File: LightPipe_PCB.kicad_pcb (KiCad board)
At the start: 4 copper layers, 38 x 38 mm, 14 parts, among them M1 2.2mm_M2, M2 2.2mm_M2, X1 AudioJack4, X2 AudioJack4, X3 XT30, X4.1 Cable-0.7mm, X4.2 Cable-0.7mm, X5.1 Cable-1.5mm, X5.2 Cable-1.5mm

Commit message: [PCB] Fixed Fab layers | added attributes to components
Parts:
- X1, X2: value AudioJack4 -> Lumberg KLB4
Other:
- rule pad_to_mask_clearance: 0.051 -> 0
- board text removed: "Rotationswinkel: 120° 60° 10°"
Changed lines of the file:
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@@
       (dielectric_constraints no)
     )
-    (pad_to_mask_clearance 0.051)
-    (solder_mask_min_width 0.25)
+    (pad_to_mask_clearance 0)
     (grid_origin 127 90)
     (pcbplotparams
@@
   (footprint "h8-Connectors:Lumberg-KLB-4-Jack-3_5-180deg-turnable" (layer "F.Cu")
     (at 138.691343 96.75 60)
+    (property "MF" "Lumberg")
+    (property "MF1" "HUXUAN")
+    (property "MFN" "KLB4")
+    (property "MFN1" "PJ392")
     (property "Sheetfile" "LightPipe_PCB.kicad_sch")
     (property "Sheetname" "")
@@
       (effects (font (size 1 1) (thickness 0.15)))
     )
-    (fp_text value "AudioJack4" (at 0 -5.5 60) (layer "F.Fab")
+    (fp_text value "Lumberg KLB4" (at 0.185417 -6.678848 60) (layer "F.Fab")
       (effects (font (size 1 1) (thickness 0.15)))
     )
@@
   (footprint "h8-Connectors:Lumberg-KLB-4-Jack-3_5-180deg-turnable" (layer "F.Cu")
     (at 115.308657 96.75 -60)
+    (property "MF" "Lumberg")
+    (property "MF1" "HUXUAN")
+    (property "MFN" "KLB4")
+    (property "MFN1" "PJ392")
     (property "Sheetfile" "LightPipe_PCB.kicad_sch")
     (property "Sheetname" "")
@@
       (effects (font (size 1 1) (thickness 0.15)))
     )
-    (fp_text value "AudioJack4" (at 0 -5.5 -60) (layer "F.Fab")
+    (fp_text value "Lumberg KLB4" (at -0.310417 -6.462341 -60) (layer "F.Fab")
       (effects (font (size 1 1) (thickness 0.15)))
     )
@@
   (footprint "h8-Connectors:XT30" (layer "F.Cu")
     (at 127 75.3)
+    (property "LCSC" "C108769")
+    (property "MF" "Changzhou Amass Elec ")
+    (property "MFN" "XT30UPB30-F.G.*")
     (property "Sheetfile" "LightPipe_PCB.kicad_sch")
     (property "Sheetname" "")
@@
       (effects (font (size 1.2 1.2) (thickness 0.2)))
     )
-    (fp_text value "XT30" (at 0 -3.7) (layer "F.Fab")
+    (fp_text value "XT30" (at 0 -3.3) (layer "F.Fab")
       (effects (font (size 0.8 0.8) (thickness 0.15)))
     )
@@
       (effects (font (size 0.8 0.8) (thickness 0.15)) (justify mirror))
     )
-    (fp_text value "Cable-1.5mm" (at 0 -7 -30 unlocked) (layer "B.Fab")
+    (fp_text value "Cable-1.5mm" (at 2.190227 -0.964746 -30 unlocked) (layer "B.Fab")
       (effects (font (size 0.8 0.8) (thickness 0.15)) (justify mirror))
     )
@@
       (effects (font (size 1 1) (thickness 0.15)) (justify mirror))
     )
-    (fp_text value "APA102" (at 4.5 -0.5 300) (layer "B.Fab")
+    (fp_text value "APA102" (at -1.17981 0.069392 300) (layer "B.Fab")
       (effects (font (size 1 1) (thickness 0.15)) (justify mirror))
     )
@@
       (effects (font (size 0.8 0.8) (thickness 0.15)) (justify mirror))
     )
-    (fp_text value "Cable-1.5mm" (at -0.1 -7 -30 unlocked) (layer "B.Fab")
+    (fp_text value "Cable-1.5mm" (at -2.189582 -1.034138 -30 unlocked) (layer "B.Fab")
       (effects (font (size 0.8 0.8) (thickness 0.15)) (justify mirror))
     )
@@
       (effects (font (size 1 1) (thickness 0.15)) (justify mirror))
     )
-    (fp_text value "APA102" (at 4.5 -0.5 180) (layer "B.Fab")
+    (fp_text value "APA102" (at -1.3 0 180) (layer "B.Fab")
       (effects (font (size 1 1) (thickness 0.15)) (justify mirror))
     )
@@
       (effects (font (size 0.8 0.8) (thickness 0.15)) (justify mirror))
     )
-    (fp_text value "Cable-0.7mm" (at 0.1 -6.400001 -30 unlocked) (layer "B.Fab")
+    (fp_text value "Cable-0.7mm" (at 0.235417 -5.775962 -30 unlocked) (layer "B.Fab")
       (effects (font (size 0.8 0.8) (thickness 0.15)) (justify mirror))
     )
@@
       (effects (font (size 0.8 0.8) (thickness 0.15)) (justify mirror))
     )
-    (fp_text value "Cable-0.7mm" (at 0.1 -6.400001 -30 unlocked) (layer "B.Fab")
+    (fp_text value "Cable-0.7mm" (at -0.208493 -5.577405 -30 unlocked) (layer "B.Fab")
       (effects (font (size 0.8 0.8) (thickness 0.15)) (justify mirror))
     )
@@
       (effects (font (size 1 1) (thickness 0.15)) (justify mirror))
     )
-    (fp_text value "APA102" (at 4.7 0 60) (layer "B.Fab")
+    (fp_text value "APA102" (at -1.30481 -0.285898 60) (layer "B.Fab")
       (effects (font (size 1 1) (thickness 0.15)) (justify mirror))
     )
@@
     (effects (font (size 0.8 0.8) (thickness 0.12)) (justify left))
   )
-  (gr_text "Rotationswinkel:\n120°\n60°\n10°" (at 149.4 85) (layer "Cmts.User")
-    (effects (font (size 0.8 0.8) (thickness 0.15)) (justify left))
-  )
   (segment (start 120.557953 105.842047) (end 116.608657 99.001666) (width 0.25) (layer "B.Cu") (net 1))

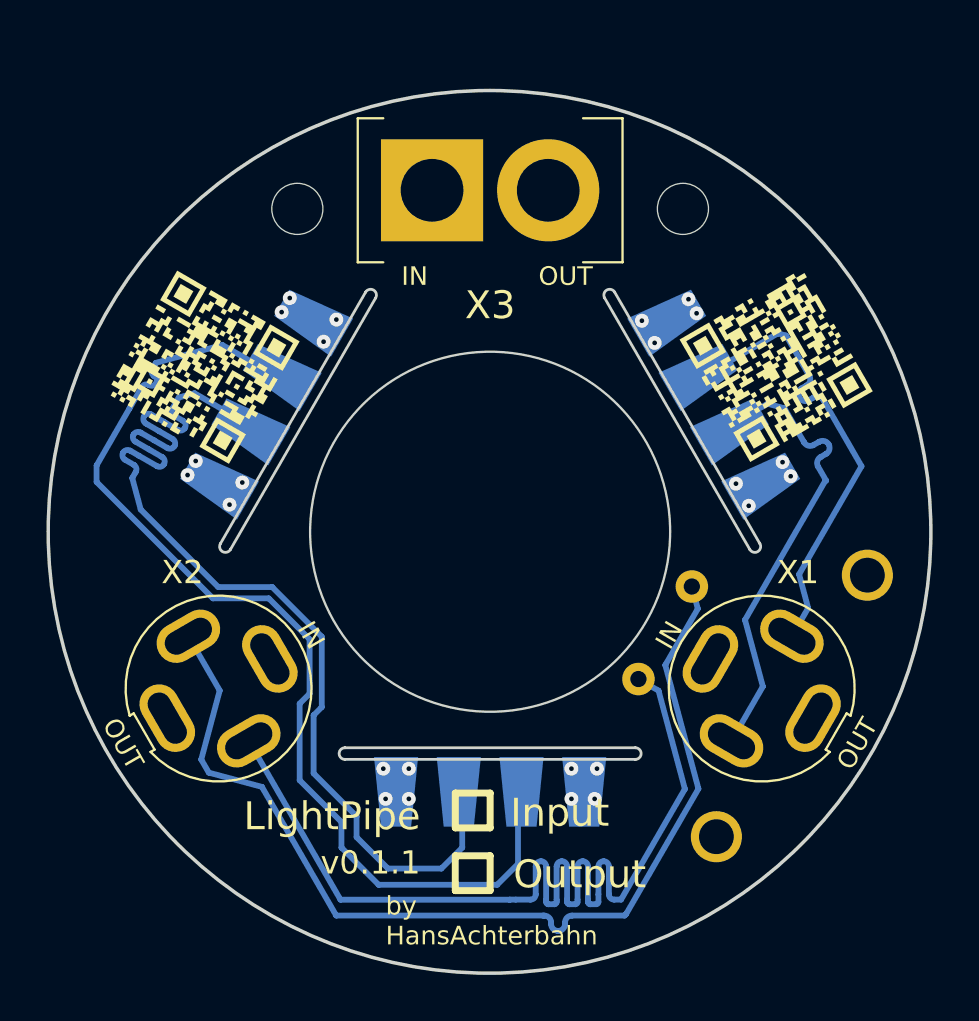
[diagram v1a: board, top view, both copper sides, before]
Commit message: [WIP] Optimize PCB for more common LED-Strip (GND, D, CLK, 5V)
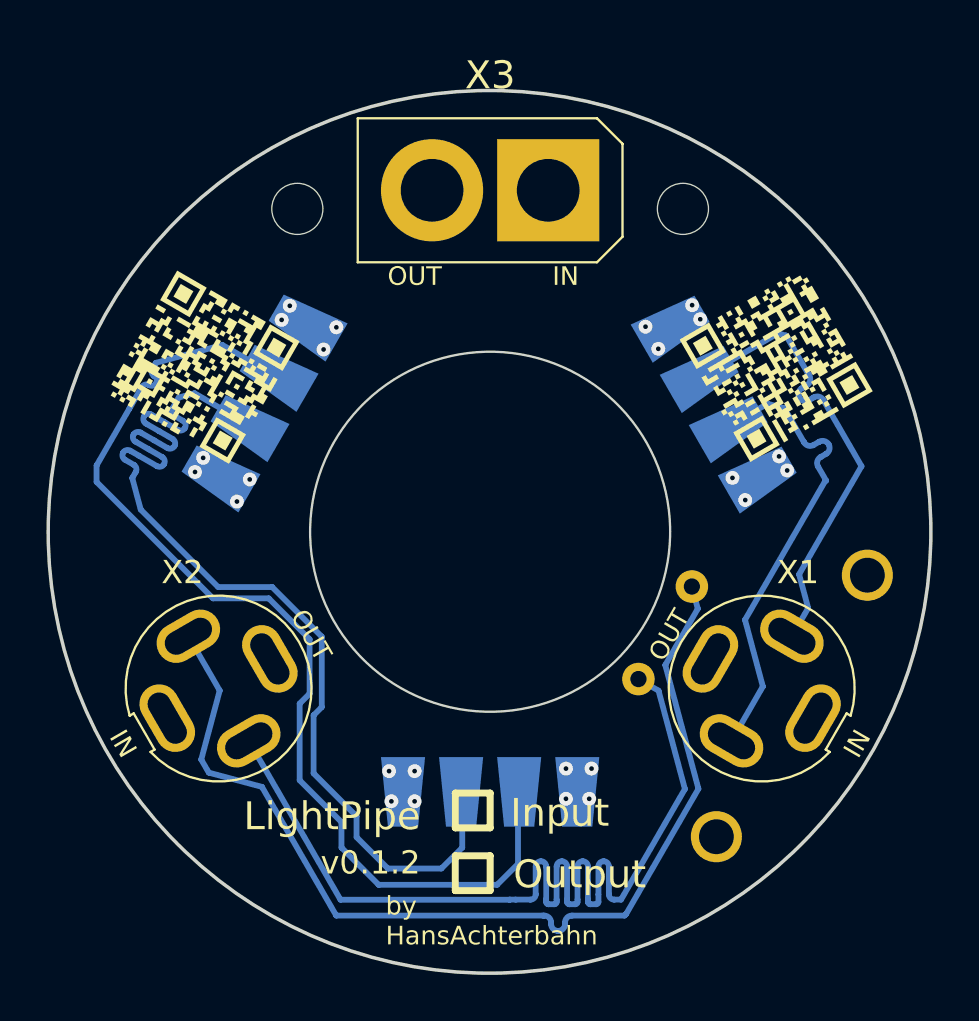
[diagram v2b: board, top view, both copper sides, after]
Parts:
- turned X3 to 180 degrees
- renumbered X5.2 to X5.1, X5.1 to X5.2
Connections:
- LD1 pad 1: +5V -> GND
- LD1 pad 2: /clk1 -> /d1
- LD1 pad 3: /d1 -> /clk1
- LD1 pad 4: GND -> +5V
- LD2 pad 1: +5V -> GND
- LD2 pad 2: /clk2 -> /d2
- LD2 pad 3: /d2 -> /clk2
- LD2 pad 4: GND -> +5V
- LD3 pad 1: +5V -> GND
- LD3 pad 2: /clk2 -> /d2
- LD3 pad 3: /d2 -> /clk2
- LD3 pad 4: GND -> +5V
- X1 pad R1: /clk1 -> /d1
- X1 pad R2: +5V -> GND
- X1 pad S: GND -> +5V
- X1 pad T: /d1 -> /clk1
- X2 pad R1: /clk3 -> /d3
- X2 pad R2: +5V -> GND
- X2 pad S: GND -> +5V
- X2 pad T: /d3 -> /clk3
- X4.1 pad 1: /clk3 -> /d3
- X4.2 pad 1: /d3 -> /clk3
- X5.1 pad 1: GND -> +5V
- X5.2 pad 1: +5V -> GND

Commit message: Optimize PCB for more common LED-Strip (GND, D, CLK, 5V) → It could be a good idea to change X4.1, X4.2, X5.1 and X5.2 to a standard footprint. There is always trouble with this custom footprints.
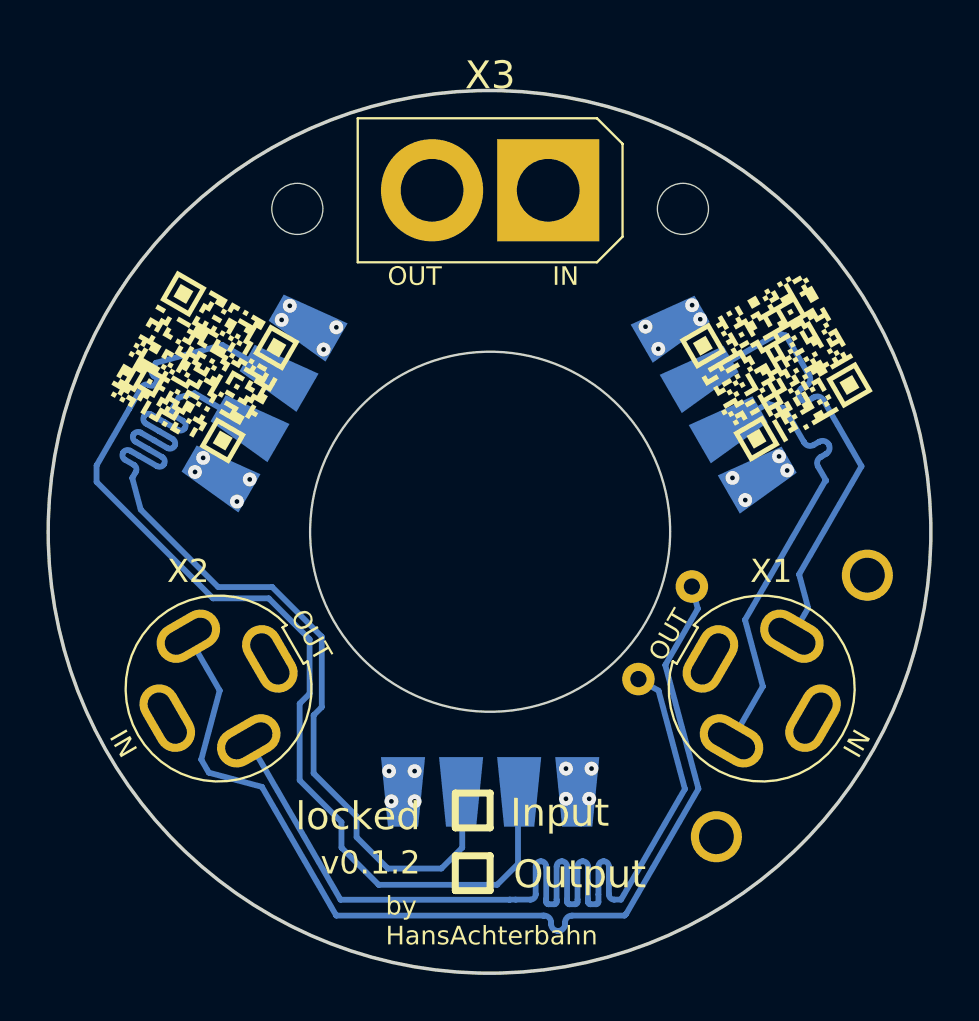
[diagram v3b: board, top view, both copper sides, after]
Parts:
- removed the X5.1 at (136.7, 103.1)
- added X5.2: Cable-1.5mm, h8-Connectors:Solder-Pad-THT-1.5mm, B.Cu at (136.7, 103.1)
- turned X1 to -120 degrees
- turned X2 to 120 degrees
- turned X5.1 to -120 degrees
- renumbered X5.2 to X5.1
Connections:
- X1 pad R1: /d1 -> /clk1
- X1 pad R2: GND -> +5V
- X1 pad S: +5V -> GND
- X1 pad T: /clk1 -> /d1
- X2 pad R1: /d3 -> /clk3
- X2 pad R2: GND -> +5V
- X2 pad S: +5V -> GND
- X2 pad T: /clk3 -> /d3
- X5.1 pad 1: GND -> +5V
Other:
- board text added: "locked"
- board text removed: "LightPipe"

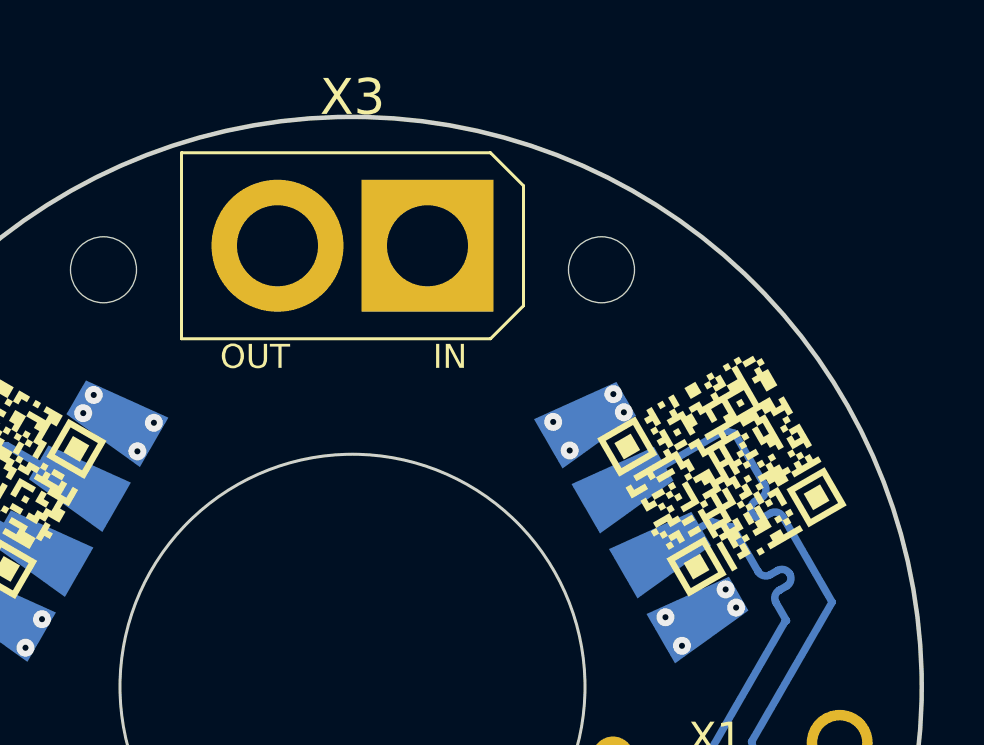
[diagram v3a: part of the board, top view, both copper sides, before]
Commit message: Try to run KiBot - but it does not work well with KiCad 7.0 → Downgrade to KiCad 6.0?
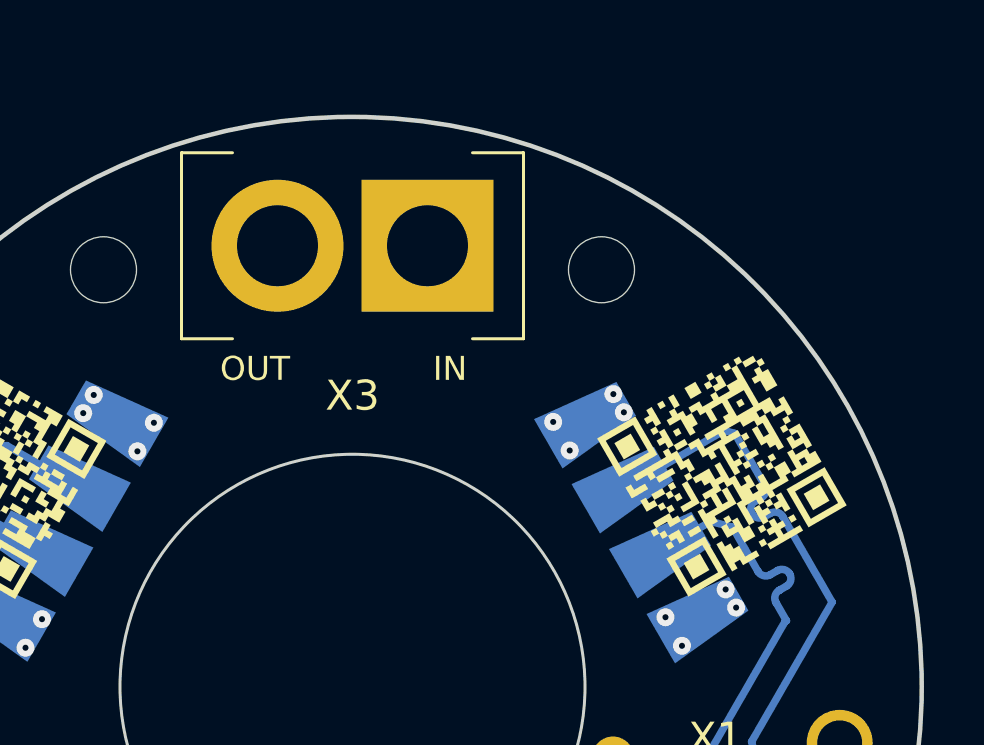
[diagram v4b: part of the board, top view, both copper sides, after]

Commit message: Optimized schematic and PCB by checking Gerber Data
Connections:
- X5.1 pad 1: +5V -> GND
- X5.2 pad 1: GND -> +5V
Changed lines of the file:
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@@
     )
     (pad "1" thru_hole circle (at 0 0 180) (size 2.2 2.2) (drill 1.5) (layers "*.Cu" "*.Mask")
-      (net 4 "+5V") (pinfunction "Pin_1") (pintype "passive") (zone_connect 1) (thermal_bridge_width 1.5))
+      (net 3 "GND") (pinfunction "Pin_1") (pintype "passive") (zone_connect 1) (thermal_bridge_width 1.5))
   )
   (footprint "h8-Connectors:APA102-Strip-Output" (layer "B.Cu")
@@
     )
     (pad "1" thru_hole circle (at 0 0 180) (size 2.2 2.2) (drill 1.5) (layers "*.Cu" "*.Mask")
-      (net 3 "GND") (pinfunction "Pin_1") (pintype "passive") (zone_connect 1) (thermal_bridge_width 1.5))
+      (net 4 "+5V") (pinfunction "Pin_1") (pintype "passive") (zone_connect 1) (thermal_bridge_width 1.5))
   )
   (footprint "h8-Connectors:Solder-Pad-THT-0.7mm" (layer "B.Cu")
@@
     (polygon
       (pts
-        (xy 152 112)
-        (xy 105.60001 112.284352)
-        (xy 105.738576 68.288425)
-        (xy 151.988566 68.029073)
+        (xy 146 109)
+        (xy 108 109)
+        (xy 108 71)
+        (xy 146 71)
       )
     )
   )
-  (zone (net 3) (net_name "GND") (layer "In2.Cu") (hatch none 0.508)
+  (zone (net 3) (net_name "GND") (layer "In2.Cu") (hatch edge 0.508)
     (connect_pads (clearance 0.3))
     (min_thickness 0.2) (filled_areas_thickness no)
@@
     (polygon
       (pts
-        (xy 155 115)
-        (xy 104 115.1375)
-        (xy 104 66)
-        (xy 155 66)
+        (xy 146 109)
+        (xy 108 109)
+        (xy 108 71)
+        (xy 146 71)
       )
     )

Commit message: [PCB] Changed Layer In1 with In2 + Kibot Export
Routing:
- added copper zone on In2.Cu, net +5V
- added copper zone on In1.Cu, net GND
- removed copper zone on In1.Cu, net +5V
- removed copper zone on In2.Cu, net GND
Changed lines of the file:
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@@
   (arc (start 112.314347 83.686298) (mid 112.143612 83.66382) (end 112.006991 83.768653) (width 0.25) (layer "B.Cu") (net 8))
   (arc (start 112.456991 82.98923) (mid 112.434513 83.159964) (end 112.539347 83.296586) (width 0.25) (layer "B.Cu") (net 8))
-  (zone (net 4) (net_name "+5V") (layer "In1.Cu") (hatch edge 0.508)
+  (zone (net 3) (net_name "GND") (layer "In1.Cu") (hatch edge 0.508)
     (connect_pads (clearance 0.3))
     (min_thickness 0.2) (filled_areas_thickness no)
@@
     )
   )
-  (zone (net 3) (net_name "GND") (layer "In2.Cu") (hatch edge 0.508)
+  (zone (net 4) (net_name "+5V") (layer "In2.Cu") (hatch edge 0.508)
     (connect_pads (clearance 0.3))
     (min_thickness 0.2) (filled_areas_thickness no)
